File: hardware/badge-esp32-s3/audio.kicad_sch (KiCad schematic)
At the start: 0 parts

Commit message: Add buzzer
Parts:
- added BUZZER1: MLT-5020, lcsc-lib:BUZ-SMD_L5.0-W5.5-P4.60, symbol lcsc-lib:MLT-5020
- added R29: 3296W-1-103, lcsc-lib:RES-ADJ-TH_3P-L10.0-W10.0-P2.50-L, symbol lcsc-lib:3296W-1-103
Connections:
- new net: BUZZER1.1 (+), R29.2
- new net 3.3V: R29.1
- new net BUZZ: BUZZER1.2 (-)
- new net GND: R29.3
- no-connect marks 0 -> 1

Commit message: Annotate schematic
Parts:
- renumbered R29 to R23
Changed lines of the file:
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@@
 		(dnp no)
 		(fields_autoplaced yes)
-		(property "Reference" "R29"
+		(property "Reference" "R23"
 			(at 149.86 81.0299 90)
 			(effects
@@
 			(project ""
 				(path "/e2af9a6c-dbe9-4de2-9ba6-ea213a7300ec/df7bf792-82c5-4feb-b2e3-af668da9099d"
-					(reference "R29")
+					(reference "R23")
 					(unit 1)
 				)
@@
 		(dnp no)
 		(fields_autoplaced yes)
-		(property "Reference" "#PWR015"
+		(property "Reference" "#PWR034"
 			(at 172.72 100.33 0)
 			(effects
@@
 			(project ""
 				(path "/e2af9a6c-dbe9-4de2-9ba6-ea213a7300ec/df7bf792-82c5-4feb-b2e3-af668da9099d"
-					(reference "#PWR015")
+					(reference "#PWR034")
 					(unit 1)
 				)

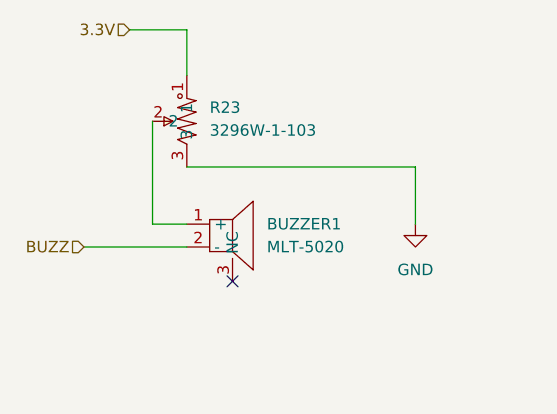
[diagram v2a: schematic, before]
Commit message: Updated the audio schematic and traces.
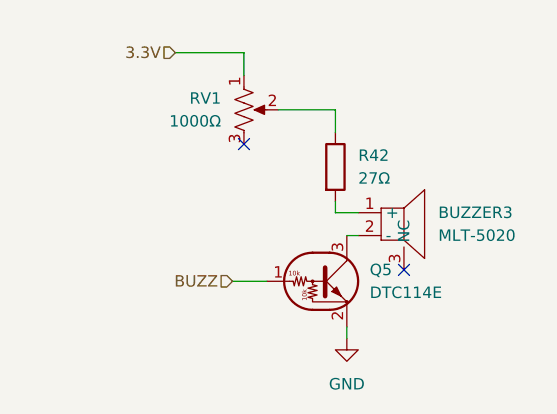
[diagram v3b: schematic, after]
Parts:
- removed BUZZER1: MLT-5020, lcsc-lib:BUZ-SMD_L5.0-W5.5-P4.60, symbol lcsc-lib:MLT-5020
- removed R23: 3296W-1-103, lcsc-lib:RES-ADJ-TH_3P-L10.0-W10.0-P2.50-L, symbol lcsc-lib:3296W-1-103
- added BUZZER3: MLT-5020, lcsc-lib:BUZ-SMD_L5.0-W5.5-P4.60, symbol lcsc-lib:MLT-5020
- added Q5: DTC114E, misc-lib:SOT-523_L1.6-W0.8-P1.00-BR, symbol Transistor_BJT:DTC114E
- added R42: 27Ω, Resistor_SMD:R_0402_1005Metric, symbol Device:R
- added RV1: 1000Ω, Potentiometer_THT:Potentiometer_Bourns_3296W_Vertical, symbol Device:R_Potentiometer_US
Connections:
- net 3.3V: now also RV1.1
- net BUZZ: now also Q5.1 (B)
- net GND: now also Q5.2 (E)
- new net: BUZZER3.1 (+), R42.2
- new net: BUZZER3.2 (-), Q5.3 (C)
- new net: R42.1, RV1.2
- no-connect marks 1 -> 2

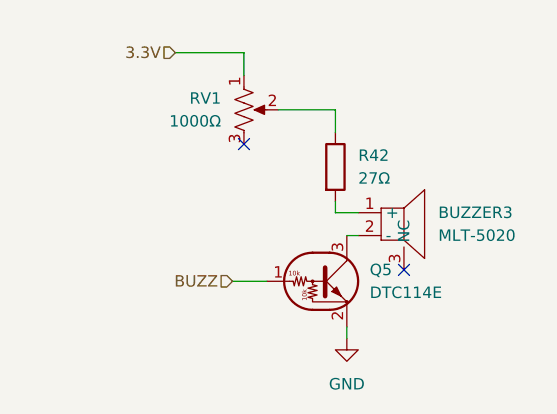
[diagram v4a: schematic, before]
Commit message: added sdio
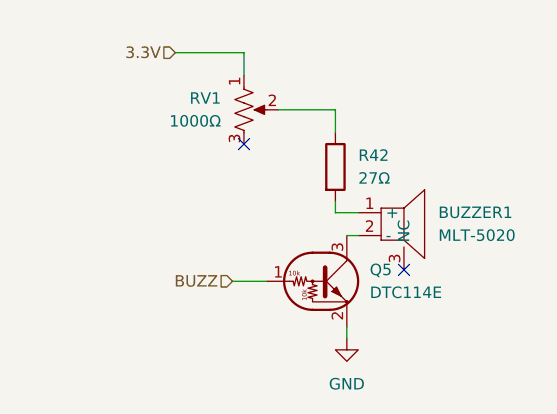
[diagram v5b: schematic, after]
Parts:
- renumbered BUZZER3 to BUZZER1
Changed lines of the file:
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@@
 		(dnp no)
 		(fields_autoplaced yes)
-		(property "Reference" "BUZZER3"
+		(property "Reference" "BUZZER1"
 			(at 175.26 92.7099 0)
 			(effects
@@
 			(project "badge-esp32-s3"
 				(path "/e2af9a6c-dbe9-4de2-9ba6-ea213a7300ec/df7bf792-82c5-4feb-b2e3-af668da9099d"
-					(reference "BUZZER3")
+					(reference "BUZZER1")
 					(unit 1)
 				)

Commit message: almost finished
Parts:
- Q5: footprint misc-lib:SOT-523_L1.6-W0.8-P1.00-BR -> misc-lib:DTC114EE
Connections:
- net 3.3V renamed 3.3v
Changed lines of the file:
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@@
 		)
 	)
-	(hierarchical_label "3.3V"
+	(hierarchical_label "3.3v"
 		(shape input)
 		(at 146.05 74.93 180)
@@
 			)
 		)
-		(property "Footprint" "misc-lib:SOT-523_L1.6-W0.8-P1.00-BR"
+		(property "Footprint" "misc-lib:DTC114EE"
 			(at 162.56 100.33 0)
 			(effects

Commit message: final changes and part updated
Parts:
- RV1: LCSC (none) -> C57089
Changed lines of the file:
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@@
+			)
+		)
+		(property "LCSC" "C57089"
+			(at 153.67 81.28 0)
+			(effects
+				(font
+					(size 1.27 1.27)
+				)
+				(hide yes)
 			)
 		)

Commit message: finished component alignment
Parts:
- Q5: LCSC (none) -> C94400
- RV1: FT Rotation Offset (none) -> -90
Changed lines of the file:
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@@
+			)
+		)
+		(property "FT Rotation Offset" "-90"
+			(at 153.67 81.28 0)
+			(effects
+				(font
+					(size 1.27 1.27)
+				)
+				(hide yes)
 			)
 		)
@@
 			(at 162.56 100.33 0)
 			(effects
+				(font
+					(size 1.27 1.27)
+				)
+				(hide yes)
+			)
+		)
+		(property "LCSC" "C94400"
+			(at 162.56 100.33 0)
+			(effects
